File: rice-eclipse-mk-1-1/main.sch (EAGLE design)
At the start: 56 parts, among them U1 LM1084ISX-5.0/NOPB, U2 THS4531IDRD8-M, U3 THS4531IDRD8-M, U4 THS4531IDRD8-M, U5 THS4531IDRD8-M, X1 2540-5

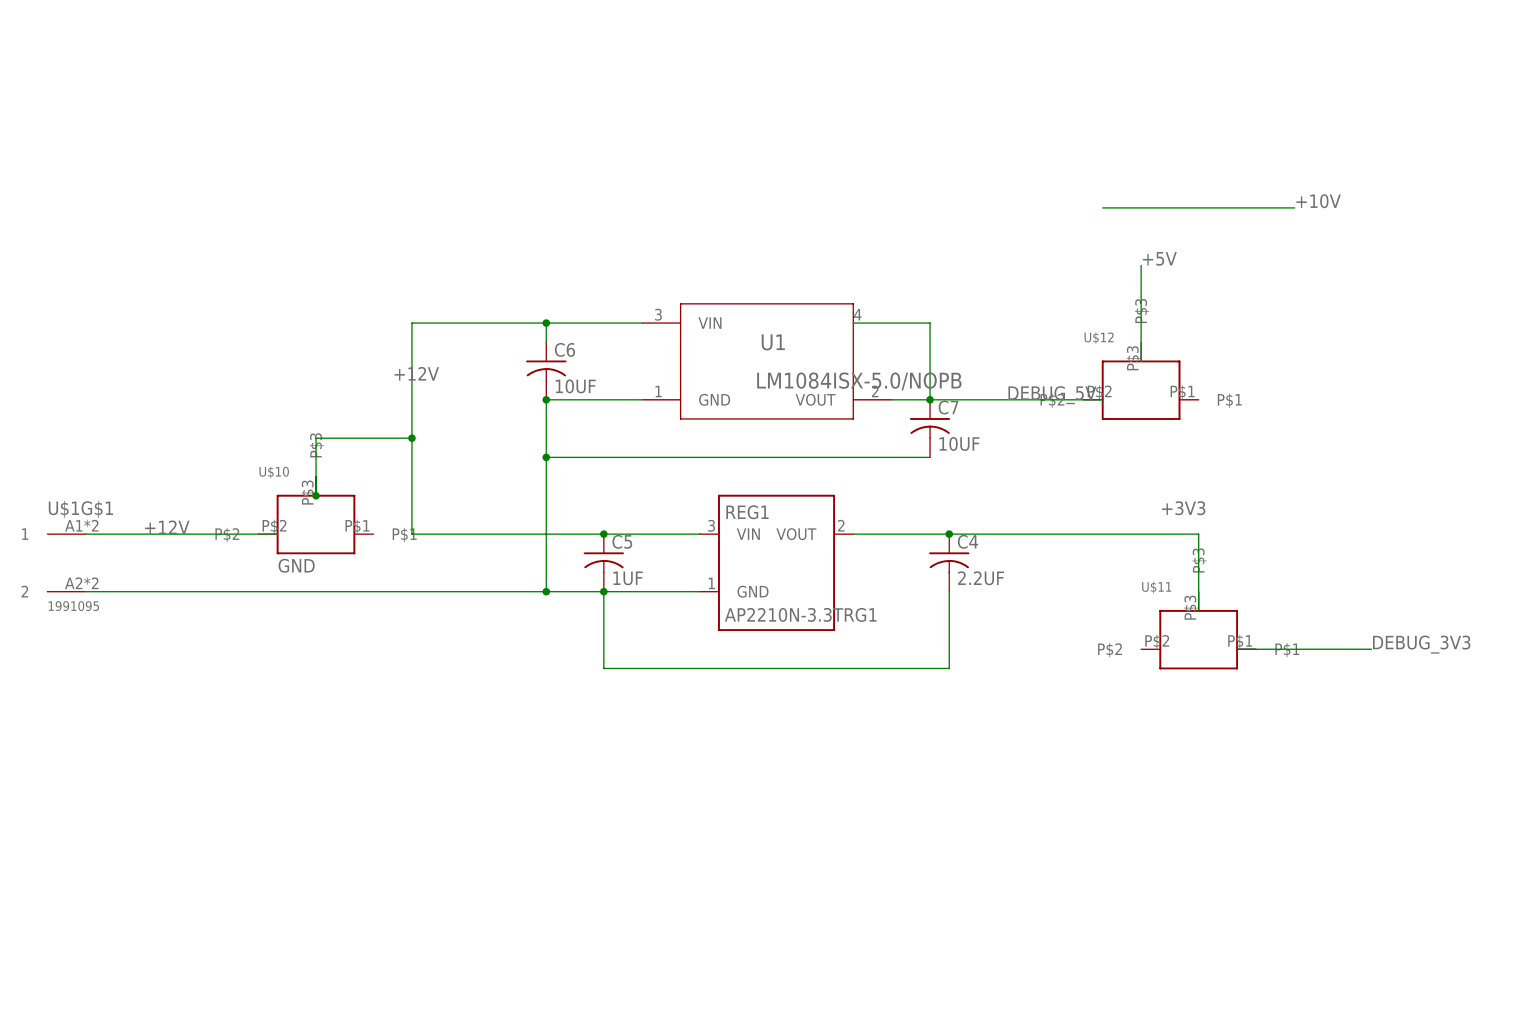
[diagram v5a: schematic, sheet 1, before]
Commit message: Added test LEDs for schematic.
LEDs allow for test of current.
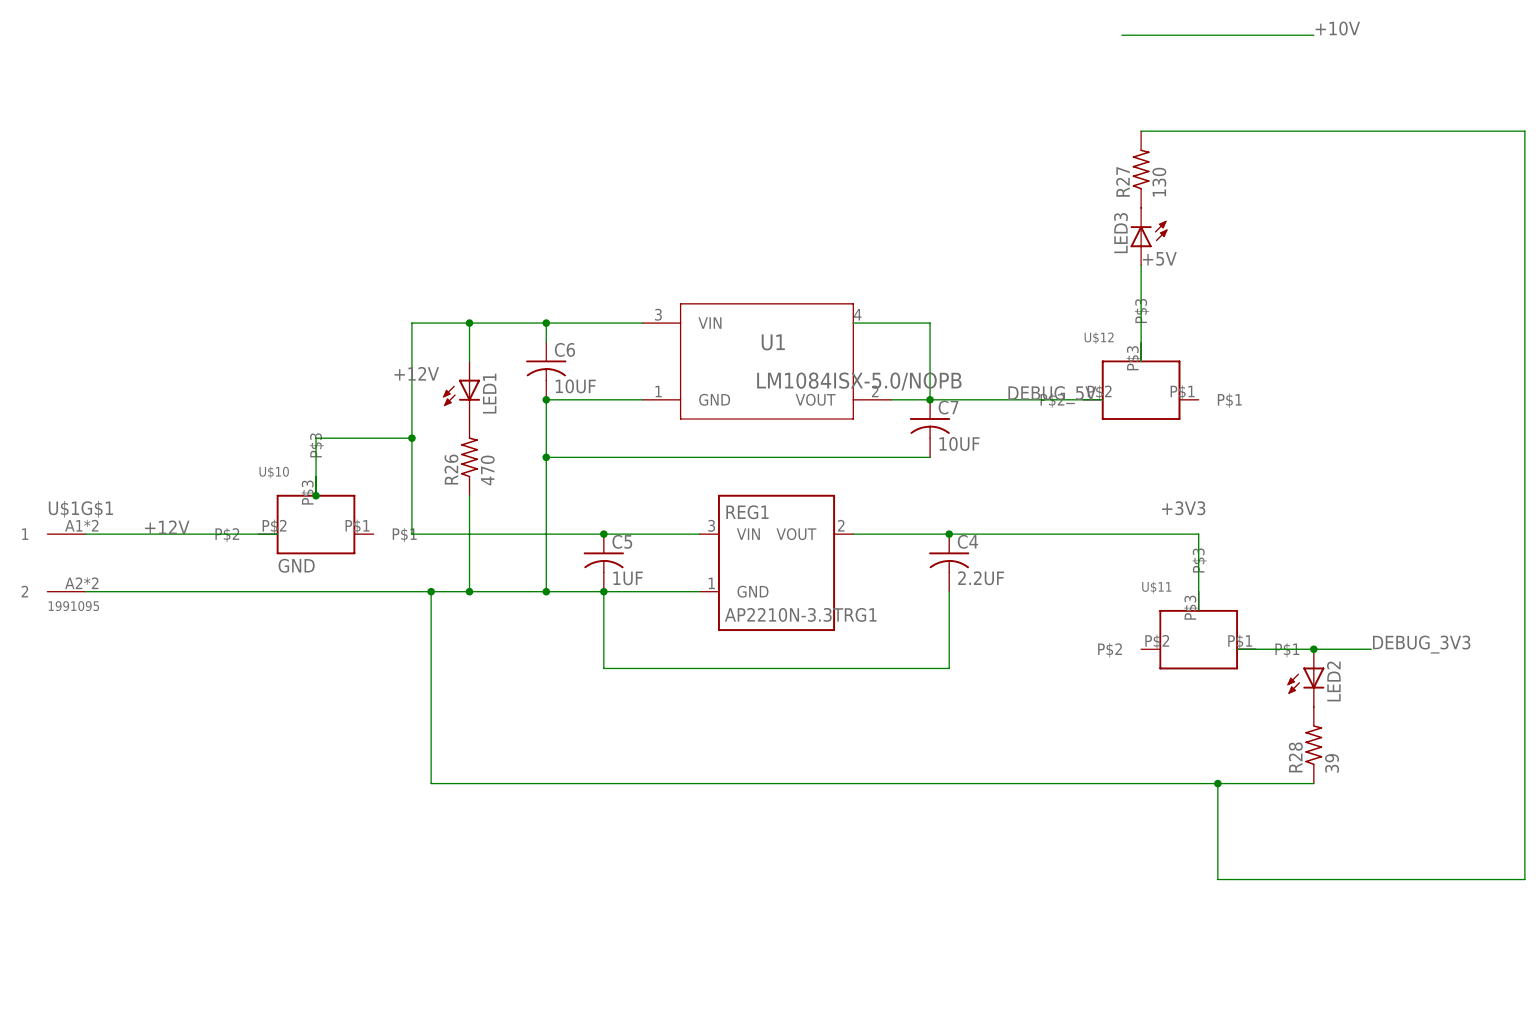
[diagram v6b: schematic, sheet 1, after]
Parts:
- added LED1, LED2, LED3: (no value), led:LED5MM
- added R26: 470, rcl:R-US_R0603
- added R27: 130, rcl:R-US_R0603
- added R28: 39, rcl:R-US_R0603
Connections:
- new net N$1: LED1.C, R26.2
- new net N$2: LED3.C, R27.1
- new net N$3: LED2.C, R28.2
- net +12V: now also LED1.A
- net +5V: now also LED3.A
- net DEBUG_3V3: now also LED2.A
- net GND: now also R26.1, R27.2, R28.1

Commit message: Deleted LEDS to resync board
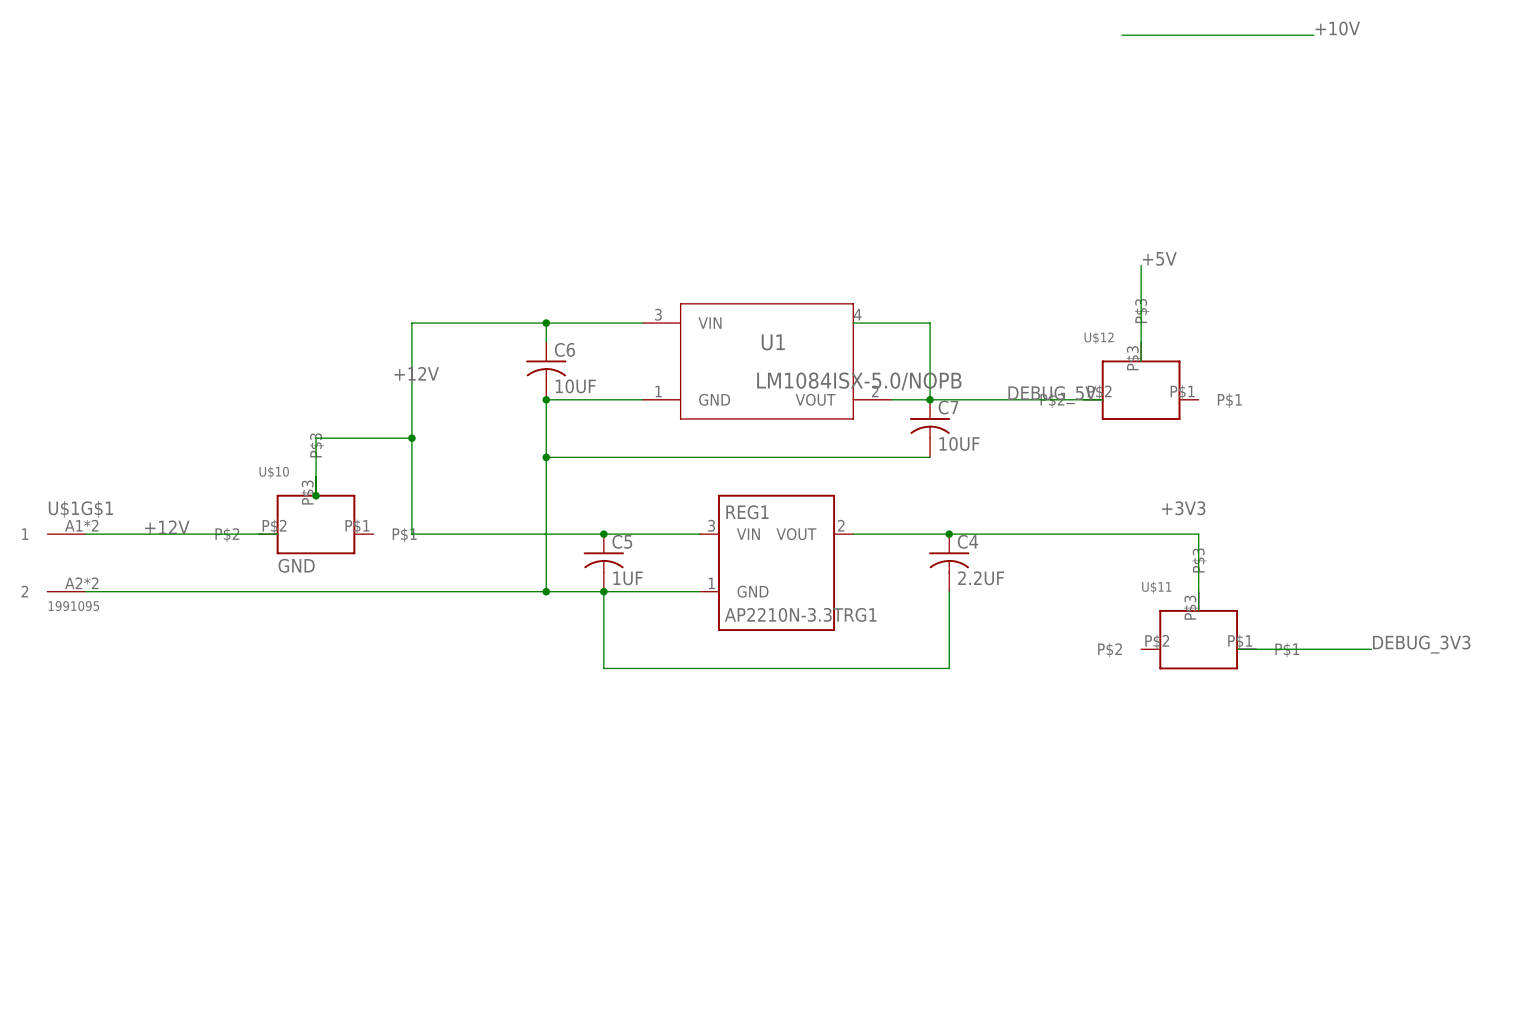
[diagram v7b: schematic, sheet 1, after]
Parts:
- removed LED1, LED2, LED3: (no value), led:LED5MM
- removed R26: 470, rcl:R-US_R0603
- removed R27: 130, rcl:R-US_R0603
- removed R28: 39, rcl:R-US_R0603
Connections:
- removed net N$1: LED1.C, R26.2
- removed net N$2: LED3.C, R27.1
- removed net N$3: LED2.C, R28.2
- net +12V: no longer LED1.A
- net +5V: no longer LED3.A
- net DEBUG_3V3: no longer LED2.A
- net GND: no longer R26.1, R27.2, R28.1
